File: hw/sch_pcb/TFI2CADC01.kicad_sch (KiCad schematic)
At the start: 21 parts, among them J1 Conn_01x05_Pin, J4 ALERT/RDY, J4 SM04B-GHS-TB, J5 SM04B-GHS-TB, U1 MIC5504-3.3YM5, U3 ADS1115IDGS

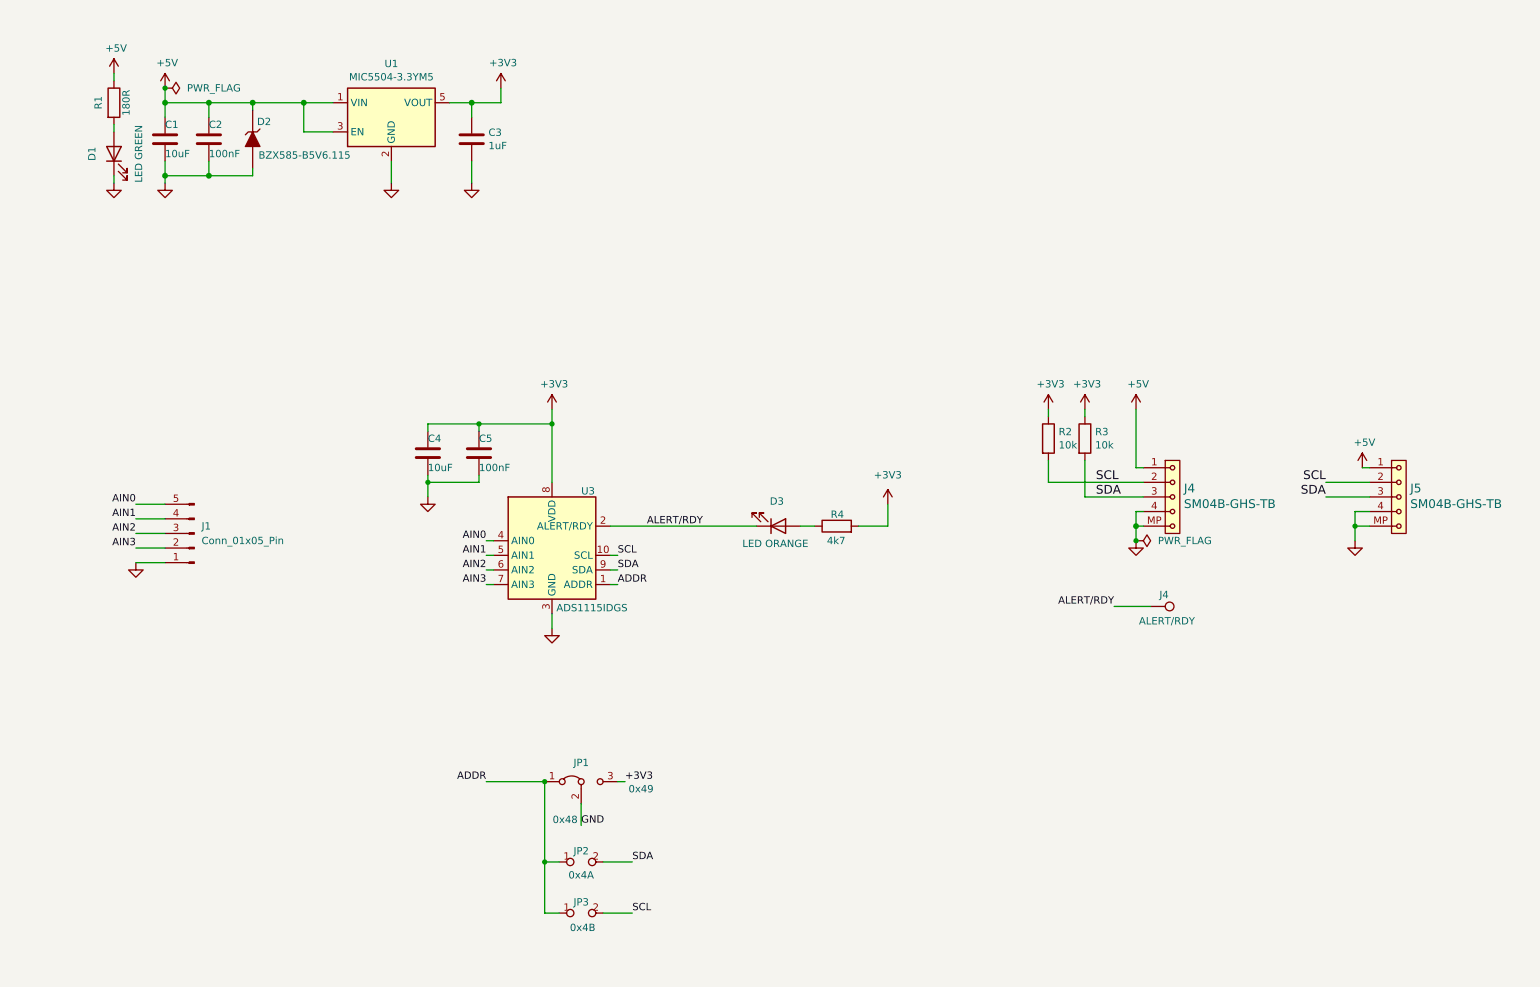
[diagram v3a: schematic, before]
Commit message: Updating footprints
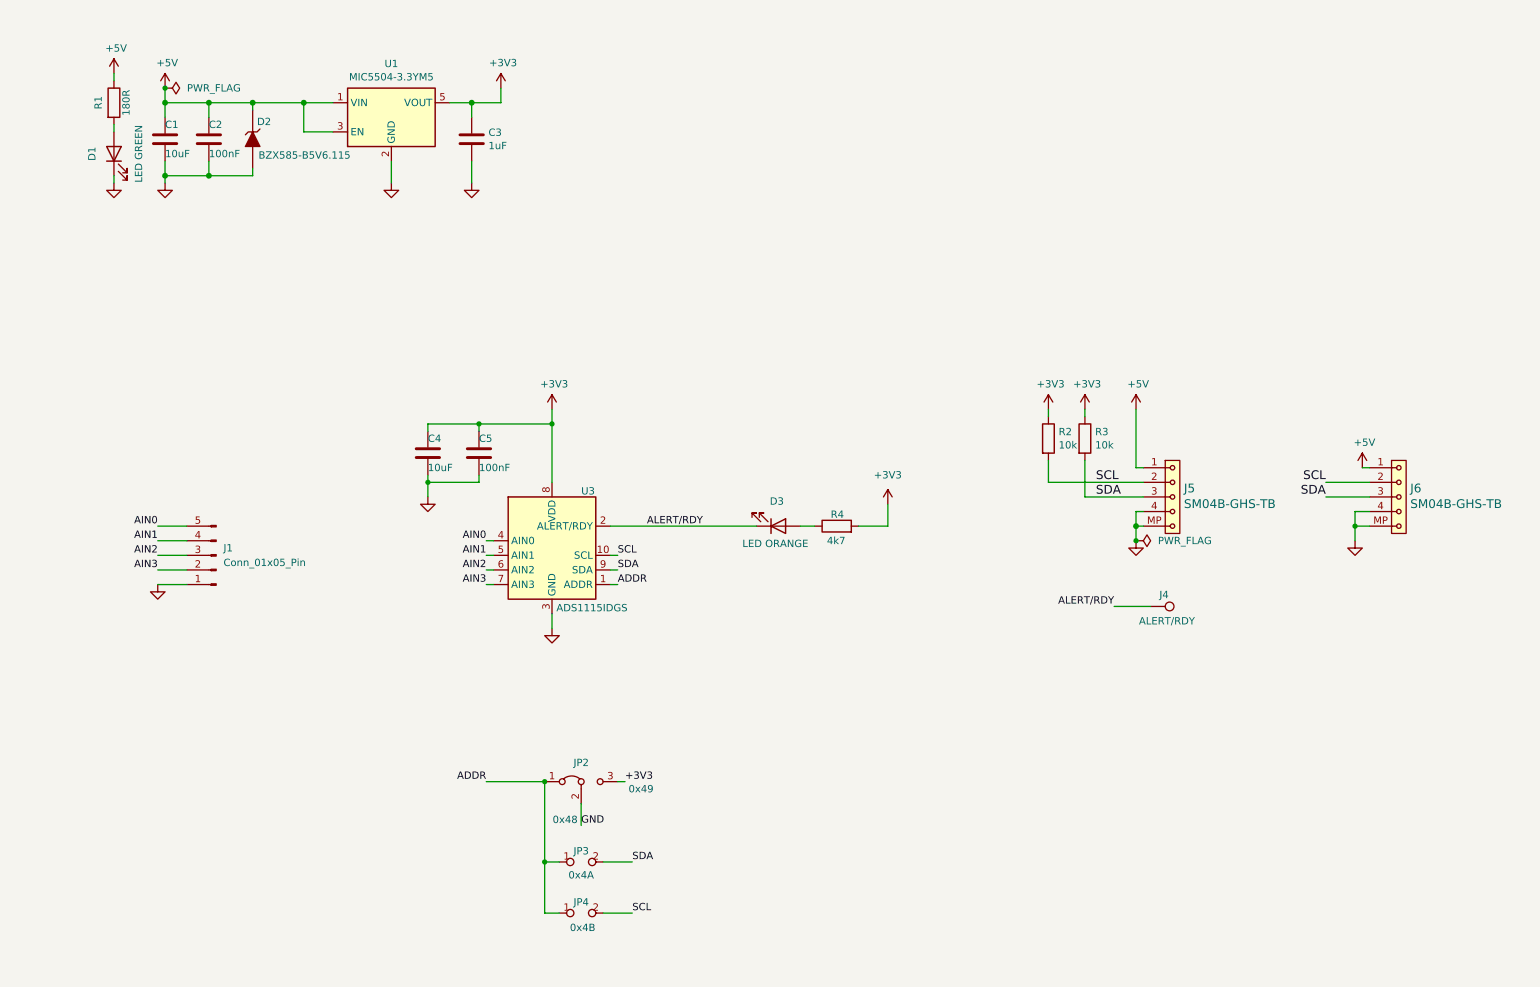
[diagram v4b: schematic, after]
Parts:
- JP3: renamed from JP2; footprint Jumper:SolderJumper-2_P1.3mm_Open_TrianglePad1.0x1.5mm -> Jumper:SolderJumper-2_P1.3mm_Open_Pad1.0x1.5mm
- JP4: renamed from JP3; footprint Jumper:SolderJumper-2_P1.3mm_Open_TrianglePad1.0x1.5mm -> Jumper:SolderJumper-2_P1.3mm_Open_Pad1.0x1.5mm
- renumbered J4 to J5, J5 to J6, JP1 to JP2
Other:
- moved on the sheet: J1
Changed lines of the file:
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@@
 	(wire
 		(pts
-			(xy 41.91 104.14) (xy 46.99 104.14)
+			(xy 45.72 107.95) (xy 50.8 107.95)
 		)
 		(stroke
@@
 	(wire
 		(pts
-			(xy 46.99 114.3) (xy 41.91 114.3)
+			(xy 50.8 118.11) (xy 45.72 118.11)
 		)
 		(stroke
@@
 	(wire
 		(pts
-			(xy 41.91 106.68) (xy 46.99 106.68)
+			(xy 45.72 110.49) (xy 50.8 110.49)
 		)
 		(stroke
@@
 	(wire
 		(pts
-			(xy 41.91 111.76) (xy 46.99 111.76)
+			(xy 45.72 115.57) (xy 50.8 115.57)
 		)
 		(stroke
@@
 	(wire
 		(pts
-			(xy 41.91 109.22) (xy 46.99 109.22)
+			(xy 45.72 113.03) (xy 50.8 113.03)
 		)
 		(stroke
@@
 	)
 	(label "AIN1"
-		(at 41.91 106.68 180)
+		(at 45.72 110.49 180)
 		(effects
 			(font
@@
 	)
 	(label "AIN2"
-		(at 41.91 109.22 180)
+		(at 45.72 113.03 180)
 		(effects
 			(font
@@
 	)
 	(label "AIN3"
-		(at 41.91 111.76 180)
+		(at 45.72 115.57 180)
 		(effects
 			(font
@@
 	)
 	(label "AIN0"
-		(at 41.91 104.14 180)
+		(at 45.72 107.95 180)
 		(effects
 			(font
@@
 		(on_board yes)
 		(dnp no)
-		(property "Reference" "J4"
+		(property "Reference" "J5"
 			(at 224.2312 101.3714 0)
 			(effects
@@
 			(project "TFI2CADC01"
 				(path "/6fb6882a-7dc1-405c-817c-bb67bd492583"
-					(reference "J4")
+					(reference "J5")
 					(unit 1)
 				)
@@
 		(on_board yes)
 		(dnp no)
-		(property "Reference" "JP1"
+		(property "Reference" "JP2"
 			(at 119.38 149.098 0)
 			(effects
@@
 			(project "TFI2CADC01"
 				(path "/6fb6882a-7dc1-405c-817c-bb67bd492583"
-					(reference "JP1")
+					(reference "JP2")
 					(unit 1)
 				)
@@
 		(on_board yes)
 		(dnp no)
-		(property "Reference" "JP2"
+		(property "Reference" "JP3"
 			(at 119.38 164.465 0)
 			(effects
@@
 			)
 		)
-		(property "Footprint" "Jumper:SolderJumper-2_P1.3mm_Open_TrianglePad1.0x1.5mm"
+		(property "Footprint" "Jumper:SolderJumper-2_P1.3mm_Open_Pad1.0x1.5mm"
 			(at 119.38 166.37 0)
 			(effects
@@
 			(project "TFI2CADC01"
 				(path "/6fb6882a-7dc1-405c-817c-bb67bd492583"
-					(reference "JP2")
+					(reference "JP3")
 					(unit 1)
 				)
@@
 	(symbol
 		(lib_id "Connector:Conn_01x05_Pin")
-		(at 52.07 109.22 180)
+		(at 55.88 113.03 180)
 		(unit 1)
 		(exclude_from_sim no)
@@
 		(fields_autoplaced yes)
 		(property "Reference" "J1"
-			(at 53.34 107.9499 0)
+			(at 57.15 111.7599 0)
 			(effects
 				(font
@@
 		)
 		(property "Value" "Conn_01x05_Pin"
-			(at 53.34 110.4899 0)
+			(at 57.15 114.2999 0)
 			(effects
 				(font
@@
 		)
 		(property "Footprint" "Connector_PinHeader_2.54mm:PinHeader_1x05_P2.54mm_Horizontal"
-			(at 52.07 109.22 0)
+			(at 55.88 113.03 0)
 			(effects
 				(font
@@
 		)
 		(property "Datasheet" "~"
-			(at 52.07 109.22 0)
+			(at 55.88 113.03 0)
 			(effects
 				(font
@@
 		)
 		(property "Description" "Generic connector, single row, 01x05, script generated"
-			(at 52.07 109.22 0)
+			(at 55.88 113.03 0)
 			(effects
 				(font
@@
 		(at 119.38 175.26 0)
 		(unit 1)
-		(exclude_from_sim no)
+		(exclude_from_sim yes)
 		(in_bom yes)
 		(on_board yes)
 		(dnp no)
-		(property "Reference" "JP3"
+		(property "Reference" "JP4"
 			(at 119.38 173.355 0)
 			(effects
@@
 			)
 		)
-		(property "Footprint" "Jumper:SolderJumper-2_P1.3mm_Open_TrianglePad1.0x1.5mm"
+		(property "Footprint" "Jumper:SolderJumper-2_P1.3mm_Open_Pad1.0x1.5mm"
 			(at 119.38 175.26 0)
 			(effects
@@
 			(project "TFI2CADC01"
 				(path "/6fb6882a-7dc1-405c-817c-bb67bd492583"
-					(reference "JP3")
+					(reference "JP4")
 					(unit 1)
 				)
@@
 	(symbol
 		(lib_id "power:GND")
-		(at 41.91 114.3 0)
+		(at 45.72 118.11 0)
 		(unit 1)
 		(exclude_from_sim no)
@@
 		(dnp no)
 		(property "Reference" "#PWR02"
-			(at 41.91 120.65 0)
+			(at 45.72 124.46 0)
 			(effects
 				(font
@@
 		)
 		(property "Value" "GND"
-			(at 42.037 118.6942 0)
+			(at 45.847 122.5042 0)
 			(effects
 				(font
@@
 		)
 		(property "Footprint" ""
-			(at 41.91 114.3 0)
+			(at 45.72 118.11 0)
 			(effects
 				(font
@@
 		)
 		(property "Datasheet" ""
-			(at 41.91 114.3 0)
+			(at 45.72 118.11 0)
 			(effects
 				(font
@@
 		)
 		(property "Description" ""
-			(at 41.91 114.3 0)
+			(at 45.72 118.11 0)
 			(effects
 				(font
@@
 		(on_board yes)
 		(dnp no)
-		(property "Reference" "J5"
+		(property "Reference" "J6"
 			(at 263.6012 101.3714 0)
 			(effects
@@
 			(project "TFI2CADC01"
 				(path "/6fb6882a-7dc1-405c-817c-bb67bd492583"
-					(reference "J5")
+					(reference "J6")
 					(unit 1)
 				)

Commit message: Updating schematics
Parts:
- removed JP2: AddresSelect, Jumper:SolderJumper-3_P1.3mm_Bridged12_Pad1.0x1.5mm_NumberLabels, symbol Jumper:Jumper_3_Bridged12
- removed JP3: 0x4A, Jumper:SolderJumper-2_P1.3mm_Open_Pad1.0x1.5mm, symbol e-radionica.com schematics:SMD_JUMPER
- removed JP4: 0x4B, Jumper:SolderJumper-2_P1.3mm_Open_Pad1.0x1.5mm, symbol e-radionica.com schematics:SMD_JUMPER
- added JP1: ~, Jumper:SolderJumper-3_P1.3mm_Bridged12_Pad1.0x1.5mm_NumberLabels, symbol Jumper:SolderJumper_3_Bridged12
- added JP2, JP3: SolderJumper_2_Open, Jumper:SolderJumper-2_P1.3mm_Open_Pad1.0x1.5mm, symbol Jumper:SolderJumper_2_Open
- renumbered J4 to J2, J5 to J3, J6 to J4
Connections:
- net +3V3: now also JP1.3 (B)
- net ADDR: now also JP1.1 (A), JP2.1 (A), JP3.1 (A)
- net GND: now also JP1.2 (C)
- net SCL: now also JP3.2 (B)
- net SDA: now also JP2.2 (B)

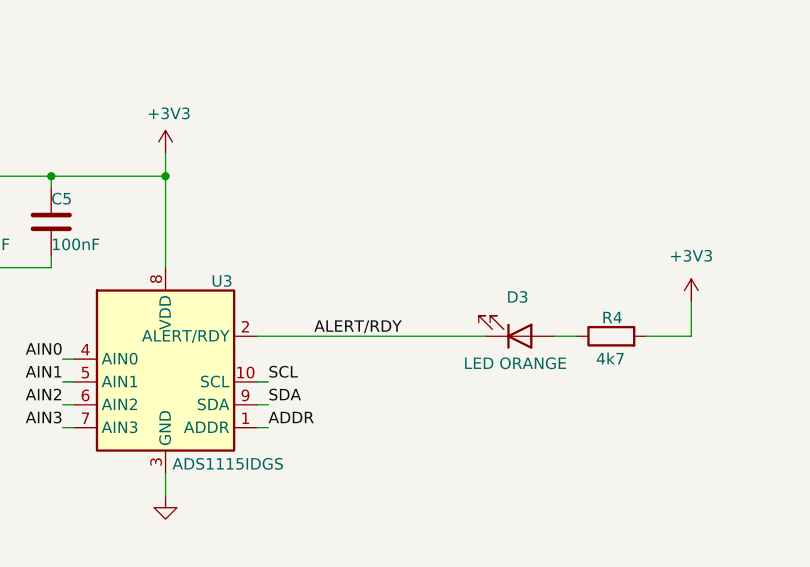
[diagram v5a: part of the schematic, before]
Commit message: Add testpoint to Alert pin.
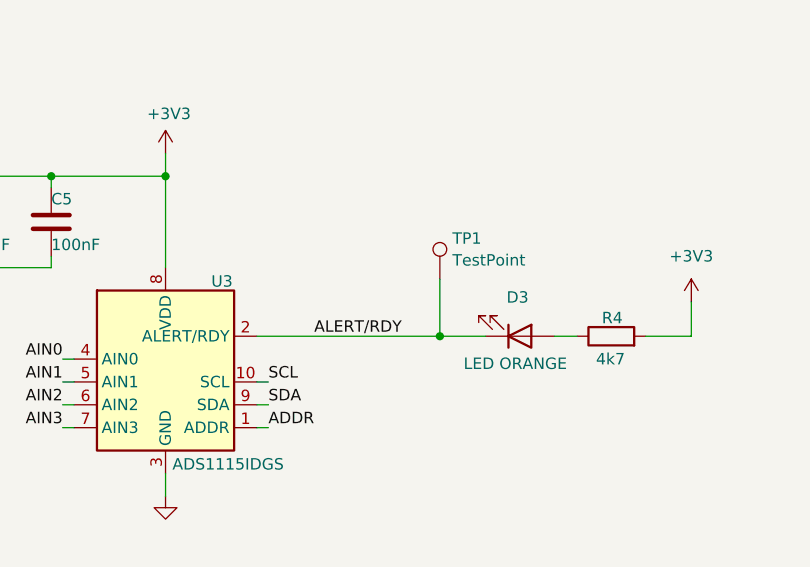
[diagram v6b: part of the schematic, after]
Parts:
- added TP1: TestPoint, symbol Connector:TestPoint
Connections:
- net ALERT/RDY: now also TP1.1
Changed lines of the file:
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@@
+	)
+	(junction
+		(at 144.78 107.95)
+		(diameter 0)
+		(color 0 0 0 0)
 	)
 	(junction
@@
 	(wire
 		(pts
+			(xy 144.78 107.95) (xy 149.86 107.95)
+		)
+		(stroke
+			(width 0)
+			(type default)
+		)
+	)
+	(wire
+		(pts
 			(xy 124.46 152.4) (xy 125.73 152.4)
 		)
@@
 	(wire
 		(pts
-			(xy 124.46 107.95) (xy 149.86 107.95)
+			(xy 124.46 107.95) (xy 144.78 107.95)
 		)
 		(stroke
@@
 			(width 0)
 			(type solid)
+		)
+	)
+	(wire
+		(pts
+			(xy 144.78 101.6) (xy 144.78 107.95)
+		)
+		(stroke
+			(width 0)
+			(type default)
 		)
 	)
@@
 					(unit 1)
 				)
+			)
+		)
+	)
+	(symbol
+		(lib_id "Connector:TestPoint")
+		(at 144.78 101.6 0)
+		(unit 1)
+		(exclude_from_sim no)
+		(in_bom yes)
+		(on_board yes)
+		(dnp no)
+		(fields_autoplaced yes)
+		(property "Reference" "TP1"
+			(at 146.177 97.0858 0)
+			(effects
+				(font
+					(size 1.27 1.27)
+				)
+				(justify left)
+			)
+		)
+		(property "Value" "TestPoint"
+			(at 146.177 99.5101 0)
+			(effects
+				(font
+					(size 1.27 1.27)
+				)
+				(justify left)
+			)
+		)
+		(property "Footprint" ""
+			(at 149.86 101.6 0)
+			(effects
+				(font
+					(size 1.27 1.27)
+				)
+				(hide yes)
+			)
+		)
+		(property "Datasheet" "~"
+			(at 149.86 101.6 0)
+			(effects
+				(font
+					(size 1.27 1.27)
+				)
+				(hide yes)
+			)
+		)
+		(property "Description" "test point"
+			(at 144.78 101.6 0)
+			(effects
+				(font
+					(size 1.27 1.27)
+				)
+				(hide yes)
+			)
+		)
+		(pin "1"
+		)
+		(instances
+			(project ""
+				(path "/6fb6882a-7dc1-405c-817c-bb67bd492583"
+					(reference "TP1")
+					(unit 1)
+				)

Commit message: Adding pcb
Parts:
- removed C4: 10uF, Mlab_R:SMD-0603, symbol Device:C
- removed J1: Conn_01x05_Pin, Connector_PinHeader_2.54mm:PinHeader_1x05_P2.54mm_Horizontal, symbol Connector:Conn_01x05_Pin
- removed JP3: SolderJumper_2_Open, Jumper:SolderJumper-2_P1.3mm_Open_Pad1.0x1.5mm, symbol Jumper:SolderJumper_2_Open
- removed TP1: TestPoint, symbol Connector:TestPoint
- added J1: HEADER_2x04, Connector_PinHeader_2.54mm:PinHeader_2x04_P2.54mm_Edge_Mount, symbol MLAB_HEADER:HEADER_2x04
- C1: footprint Mlab_R:SMD-0603 -> Mlab_R:SMD-0805
- renumbered C5 to C4, J3 to J2, J4 to J3, J2 to T1, U3 to U2
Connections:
- net ADDR: now also JP1.2 (C); no longer JP1.1 (A)
- net AIN0: now also J1.5
- net AIN1: now also J1.3
- net AIN2: now also J1.4
- net AIN3: now also J1.6
- net GND: now also JP1.1 (A), J1.1, J1.2, J1.7, J1.8; no longer JP1.2 (C)
- net SCL: now also JP2.2 (B)
- net SDA: no longer JP2.2 (B)
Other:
- note removed: "0x4A"
- moved on the sheet: JP1, T1
